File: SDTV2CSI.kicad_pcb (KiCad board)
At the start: 4 copper layers, 65 x 21 mm, 43 parts, among them J1 Conn_Coaxial, J2 Conn_Coaxial, J3 SFW15R-1STE1LF, U1 ADV7280AWBCPZ-M, U2 TLV75718PDBV, Y1 28.63636MHz

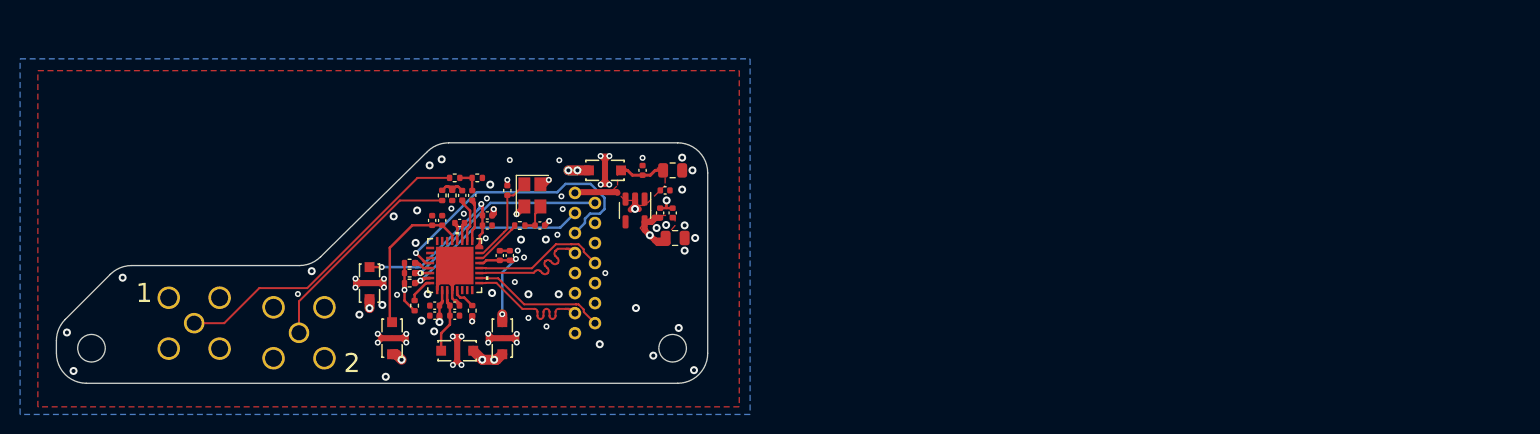
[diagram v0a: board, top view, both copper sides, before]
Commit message: update and considering losing poe for waveshare OTS
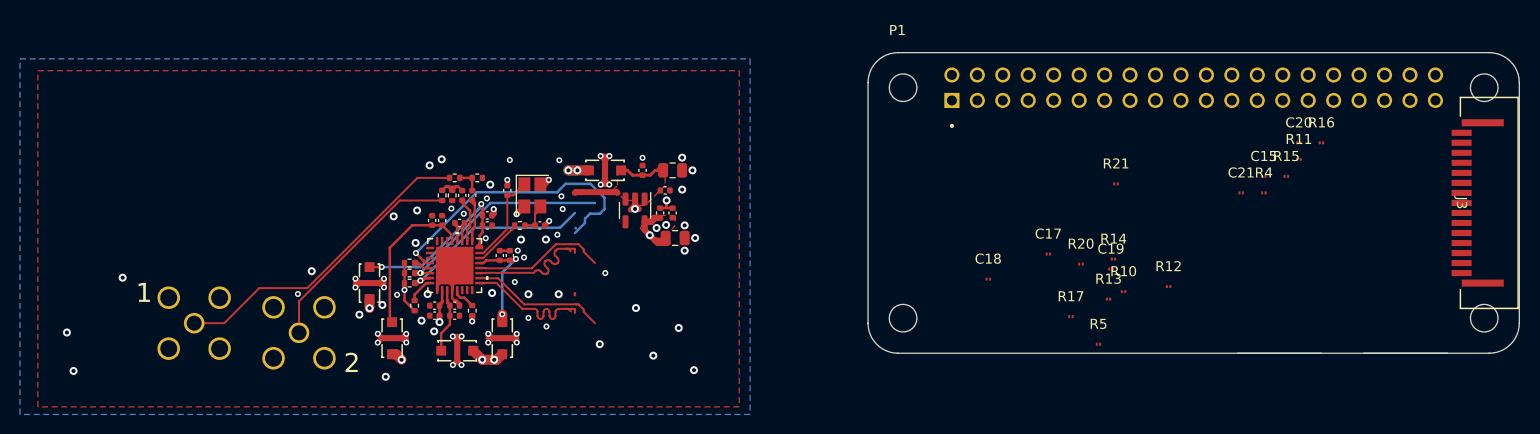
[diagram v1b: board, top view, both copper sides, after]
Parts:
- removed REF**: MODULE_ADA3708, AU:PIZERO_OUTLINE
- added C15: 0.1μF, AU:R_0201_0603Metric, F.Cu at (219.2, 52.4)
- added C17: 0.1μF, AU:R_0201_0603Metric, F.Cu at (197.8, 60.1)
- added C18: 0.1μF, AU:R_0201_0603Metric, F.Cu at (191.8, 62.6)
- added C19: 0.1μF, AU:R_0201_0603Metric, F.Cu at (204.0, 61.6)
- added C20: 0.1μF, AU:R_0201_0603Metric, F.Cu at (222.8, 49.0)
- added C21: 0.1μF, AU:R_0201_0603Metric, F.Cu at (217.0, 54.0)
- added P1: Pi Zero, AU:PIZERO, F.Cu at (212.2, 55.0)
- added R10: 24, Resistor_SMD:R_0201_0603Metric, F.Cu at (205.2, 63.9)
- added R11: 51, Resistor_SMD:R_0201_0603Metric, F.Cu at (222.8, 50.6)
- added R12: 24, Resistor_SMD:R_0201_0603Metric, F.Cu at (209.8, 63.4)
- added R13: 51, Resistor_SMD:R_0201_0603Metric, F.Cu at (203.8, 64.6)
- added R14: 24, Resistor_SMD:R_0201_0603Metric, F.Cu at (204.2, 60.6)
- added R15: 51, Resistor_SMD:R_0201_0603Metric, F.Cu at (221.5, 52.4)
- added R16: 24, Resistor_SMD:R_0201_0603Metric, F.Cu at (225.0, 49.0)
- added R17: 51, Resistor_SMD:R_0201_0603Metric, F.Cu at (200.0, 66.3)
- added R20: 24, Resistor_SMD:R_0201_0603Metric, F.Cu at (201.0, 61.1)
- added R21: 51, Resistor_SMD:R_0201_0603Metric, F.Cu at (204.5, 53.1)
- added R4: 24, Resistor_SMD:R_0201_0603Metric, F.Cu at (219.2, 54.0)
- added R5: 51, Resistor_SMD:R_0201_0603Metric, F.Cu at (202.8, 69.1)
- J3: footprint AU:528061510 -> AU:CON15_1X15_DRB_SFW_GLE; moved to F.Cu
- moved J3 90.4 mm to (241.8, 55.0), turned to -90 degrees
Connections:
- net SCL renamed CSCL
- net SDA renamed CSDA
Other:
- board size 65 x 21 mm -> 65 x 30 mm

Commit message: working on converting back to 0201
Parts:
- added J4: Conn_Coaxial, Connector_Coaxial:SMA_Amphenol_901-144_Vertical, F.Cu at (207.2, 97.8)
- added J5: Conn_Coaxial, Connector_Coaxial:SMA_Amphenol_901-144_Vertical, F.Cu at (178.8, 123.5)
- added J6: Conn_Coaxial, Connector_Coaxial:SMA_Amphenol_901-144_Vertical, F.Cu at (207.2, 107.2)
- added J7: Conn_Coaxial, Connector_Coaxial:SMA_Amphenol_901-144_Vertical, F.Cu at (196.2, 113.0)
- added J8: Conn_Coaxial, Connector_Coaxial:SMA_Amphenol_901-144_Vertical, F.Cu at (188.1, 122.4)
- added J9: Conn_Coaxial, Connector_Coaxial:SMA_Amphenol_901-144_Vertical, F.Cu at (186.9, 113.0)
- added R27: 4.7k, Resistor_SMD:R_0402_1005Metric, F.Cu at (162.5, 85.5)
- added R28: 4.7k, Resistor_SMD:R_0402_1005Metric, F.Cu at (144.1, 94.5)
- added R29: 4.7k, Resistor_SMD:R_0402_1005Metric, F.Cu at (138.2, 94.5)
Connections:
- U1 pad 6: unconnected-(U1-Pad6) -> Net-(U1-Pad6)
- U1 pad 7: unconnected-(U1-Pad7) -> Net-(U1-Pad7)
- U1 pad 8: unconnected-(U1-Pad8) -> Net-(U1-Pad8)

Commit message: will remove PoE components commit for posterity
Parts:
- C1, C10, C11, C12, C13, C14, C16, C2, C3, C4, C5, C6, C7, C8, C9: footprint Capacitor_SMD:C_0402_1005Metric -> AU:R_0201_0603Metric
- J3: moved to B.Cu
- R1, R2, R24, R25, R26, R27, R28, R29, R3, R6, R7, R9: footprint Resistor_SMD:R_0402_1005Metric -> Resistor_SMD:R_0201_0603Metric
- R23: footprint Resistor_SMD:R_0402_1005Metric -> AU:R_0201_0603Metric
- U2: value TLV75718PDBV -> TLV75718
- turned J3 to 90 degrees
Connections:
- C10 pad 1: GND -> PVDD
- C10 pad 2: PVDD -> GND
- C12 pad 1: GND -> AVDD
- C12 pad 2: AVDD -> GND
- C13 pad 1: Net-(C13-Pad1) -> Net-(U1-Pad20)
- C13 pad 2: Net-(C13-Pad2) -> Net-(U1-Pad19)
- C14 pad 2: Net-(C14-Pad2) -> Net-(R2-Pad2)
- C15 pad 2: Net-(C15-Pad2) -> Net-(R5-Pad2)
- C16 pad 2: Net-(C16-Pad2) -> Net-(R9-Pad2)
- C2 pad 1: GND -> DVDDIO
- C2 pad 2: DVDDIO -> GND
- C5 pad 1: GND -> MVDD
- C5 pad 2: MVDD -> GND
- C8 pad 1: GND -> DVDD
- C8 pad 2: DVDD -> GND
- J3 pad 1: GND -> +3V3
- J3 pad 10: GND -> CD1+
- J3 pad 11: PWR_EN -> CD1-
- J3 pad 12: LED_EN -> GND
- J3 pad 13: CSCL -> CD0+
- J3 pad 14: CSDA -> CD0-
- J3 pad 15: +3V3 -> GND
- J3 pad 2: CD0- -> CSDA
- J3 pad 3: CD0+ -> CSCL
- J3 pad 4: GND -> LED_EN
- J3 pad 5: CD1- -> PWR_EN
- J3 pad 6: CD1+ -> GND
- J3 pad 7: GND -> CLK+
- J3 pad 9: CLK+ -> GND
- R1 pad 1: Net-(R1-Pad1) -> DVDDIO
- R1 pad 2: DVDDIO -> Net-(U1-Pad29)
- R11 pad 1: Net-(C17-Pad2) -> GND
- R11 pad 2: GND -> Net-(C17-Pad2)
- R13 pad 1: Net-(C18-Pad2) -> GND
- R13 pad 2: GND -> Net-(C18-Pad2)
- R15 pad 1: Net-(C19-Pad2) -> GND
- R15 pad 2: GND -> Net-(C19-Pad2)
- R17 pad 1: Net-(C20-Pad2) -> GND
- R17 pad 2: GND -> Net-(C20-Pad2)
- R2 pad 2: Net-(C14-Pad2) -> Net-(R2-Pad2)
- R21 pad 1: Net-(C21-Pad2) -> GND
- R21 pad 2: GND -> Net-(C21-Pad2)
- R25 pad 1: CSDA -> DVDDIO
- R25 pad 2: DVDDIO -> CSDA
- R26 pad 1: INTRQ -> DVDDIO
- R26 pad 2: DVDDIO -> INTRQ
- R27 pad 1: Net-(U1-Pad7) -> Net-(R27-Pad1)
- R28 pad 1: Net-(U1-Pad6) -> Net-(R28-Pad1)
- R29 pad 1: Net-(U1-Pad8) -> GND
- R29 pad 2: GND -> Net-(U1-Pad8)
- R3 pad 1: Net-(C14-Pad2) -> GND
- R3 pad 2: GND -> Net-(R2-Pad2)
- R4 pad 2: Net-(C15-Pad2) -> Net-(R5-Pad2)
- R5 pad 1: Net-(C15-Pad2) -> GND
- R5 pad 2: GND -> Net-(R5-Pad2)
- R7 pad 2: Net-(C16-Pad2) -> Net-(R9-Pad2)
- R9 pad 1: Net-(C16-Pad2) -> GND
- R9 pad 2: GND -> Net-(R9-Pad2)
- U1 pad 19: Net-(C13-Pad1) -> Net-(U1-Pad19)
- U1 pad 20: Net-(C13-Pad2) -> Net-(U1-Pad20)
- U1 pad 29: Net-(R1-Pad1) -> Net-(U1-Pad29)
- U1 pad 6: Net-(U1-Pad6) -> Net-(R27-Pad1)
- U1 pad 7: Net-(U1-Pad7) -> Net-(R28-Pad1)
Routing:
- net DVDDIO: track 50.4 -> 72.8 mm, vias 5 -> 6
- net CSDA: track 22.4 -> 0.00 mm, vias 1 -> 0
- net Net-(U1-Pad29): track 0.00 -> 2.54 mm
- net Net-(R1-Pad1): track 2.54 -> 0.00 mm
- net Net-(U1-Pad20): track 0.00 -> 2.46 mm
- net Net-(C13-Pad2): track 2.46 -> 0.00 mm
- net Net-(U1-Pad19): track 0.00 -> 2.31 mm
- net Net-(C13-Pad1): track 2.31 -> 0.00 mm
- net PVDD: track 21.0 -> 21.8 mm
- net GND: track 52.0 -> 51.2 mm

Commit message: updating for GitHub
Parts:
- removed J3: SFW15R-1STE1LF, AU:CON15_1X15_DRB_SFW_GLE
- removed J4, J5, J6, J7, J8: Conn_Coaxial, Connector_Coaxial:SMA_Amphenol_901-144_Vertical
- added D1: TVS, AU:R_0201_0603Metric, F.Cu at (103.8, 96.2)
- added D10: TVS, AU:R_0201_0603Metric, F.Cu at (103.8, 97.9)
- added D11: TVS, AU:R_0201_0603Metric, F.Cu at (106.0, 97.9)
- added D12: TVS, AU:R_0201_0603Metric, F.Cu at (108.2, 99.5)
- added D13: TVS, AU:R_0201_0603Metric, F.Cu at (103.4, 102.8)
- added D14: TVS, AU:R_0201_0603Metric, F.Cu at (108.2, 97.9)
- added D15: TVS, AU:R_0201_0603Metric, F.Cu at (108.2, 96.2)
- added D16: TVS, AU:R_0201_0603Metric, F.Cu at (103.4, 101.2)
- added D17: TVS, AU:R_0201_0603Metric, F.Cu at (105.6, 101.2)
- added D18: LED_Dual_AAK, Package_TO_SOT_SMD:SOT-23, F.Cu at (98.0, 96.5)
- added D2: TVS, AU:R_0201_0603Metric, F.Cu at (106.0, 96.2)
- added D3: TVS, AU:R_0201_0603Metric, F.Cu at (106.0, 99.5)
- added D4: TVS, AU:R_0201_0603Metric, F.Cu at (98.9, 102.3)
- added D5: 3VWM, AU:R_0201_0603Metric, F.Cu at (101.1, 102.3)
- added D6: 3VWM, AU:R_0201_0603Metric, F.Cu at (98.9, 100.7)
- added D7: 3VWM, AU:R_0201_0603Metric, F.Cu at (103.8, 99.5)
- added D8: 3VWM, AU:R_0201_0603Metric, F.Cu at (101.1, 100.7)
- added D9: 3VWM, AU:R_0201_0603Metric, F.Cu at (110.5, 96.2)
- added R18: 560, AU:R_0201_0603Metric, F.Cu at (95.2, 96.5)
- added R19: 220, AU:R_0201_0603Metric, F.Cu at (95.2, 97.2)
- added R8: 560, AU:R_0201_0603Metric, F.Cu at (95.2, 95.8)
- added U3: TCA9555RGER, Package_DFN_QFN:VQFN-24-1EP_4x4mm_P0.5mm_EP2.45x2.45mm, F.Cu at (193.7, 27.8)
- added U4: TS3DS10224RUK, Package_DFN_QFN:WQFN-20-1EP_3x3mm_P0.4mm_EP1.7x1.7mm_ThermalVias, F.Cu at (206.0, 31.0)
- added U5: TS3DS10224RUK, Package_DFN_QFN:WQFN-20-1EP_3x3mm_P0.4mm_EP1.7x1.7mm_ThermalVias, F.Cu at (200.7, 25.7)
- added U6: TS3DS10224RUK, Package_DFN_QFN:WQFN-20-1EP_3x3mm_P0.4mm_EP1.7x1.7mm_ThermalVias, F.Cu at (200.7, 31.0)
- added U7: TS3DS10224RUK, Package_DFN_QFN:WQFN-20-1EP_3x3mm_P0.4mm_EP1.7x1.7mm_ThermalVias, F.Cu at (206.0, 25.7)
- F1, F2, F3, F4, F5: value LC(PI) -> LC(Pi); footprint AU:NFE31PT101C1E9L_MUR -> AU:MEM1608P25R0T001
- J1, J2: value Conn_Coaxial -> SMA
- J9: value Conn_Coaxial -> SFW15R-1STE1LF; footprint Connector_Coaxial:SMA_Amphenol_901-144_Vertical -> AU:CON15_1X15_DRB_SFW_GLE
- P1: moved to B.Cu
- moved J9 75.8 mm to (235.8, 55.0), turned to -90 degrees
- moved C12 49.4 mm to (185.0, 48.8), turned to 0 degrees
- moved C11 47.4 mm to (184.0, 49.0)
- moved C2 46.9 mm to (182.8, 58.2), turned to 180 degrees
- moved C1 46.9 mm to (182.8, 57.5)
- moved U1 46.6 mm to (184.5, 53.5)
- moved C13 46.6 mm to (185.0, 49.5), turned to 0 degrees
- moved C8 46.4 mm to (184.2, 58.2), turned to 0 degrees
- moved C6 46.4 mm to (184.2, 57.5)
- moved C9 46.2 mm to (187.2, 49.5)
- moved C10 46.1 mm to (187.2, 48.8)
- moved C3 45.9 mm to (188.2, 52.8)
- moved C5 45.6 mm to (189.0, 52.8)
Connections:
- F1 pad 1: DVDDIO -> +3V3
- F1 pad 3: +3V3 -> DVDDIO
- F2 pad 1: MVDD -> +1V8
- F2 pad 3: +1V8 -> MVDD
- F3 pad 1: DVDD -> +1V8
- F3 pad 3: +1V8 -> DVDD
- F4 pad 1: PVDD -> +1V8
- F4 pad 3: +1V8 -> PVDD
- F5 pad 1: AVDD -> +1V8
- F5 pad 3: +1V8 -> AVDD
- J9 pad 1: video_in4 -> +3V3
- J9 pad 2: GND -> CSDA
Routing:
- net AVDD: track 15.7 -> 11.3 mm
- net video2: track 4.95 -> 1.17 mm
- net video1: track 4.79 -> 1.05 mm
- net Net-(C16-Pad2) (its old number): track 3.55 -> 0.00 mm
- net video_in1: track 31.5 -> 28.3 mm
- net Net-(C14-Pad2) (its old number): track 2.50 -> 0.00 mm
- net Net-(C13-Pad1): track 2.46 -> 1.18 mm
- net Net-(C13-Pad2): track 2.31 -> 1.38 mm
- net PVDD: track 21.8 -> 21.0 mm
- net GND: track 51.2 -> 52.0 mm, vias 77 -> 76

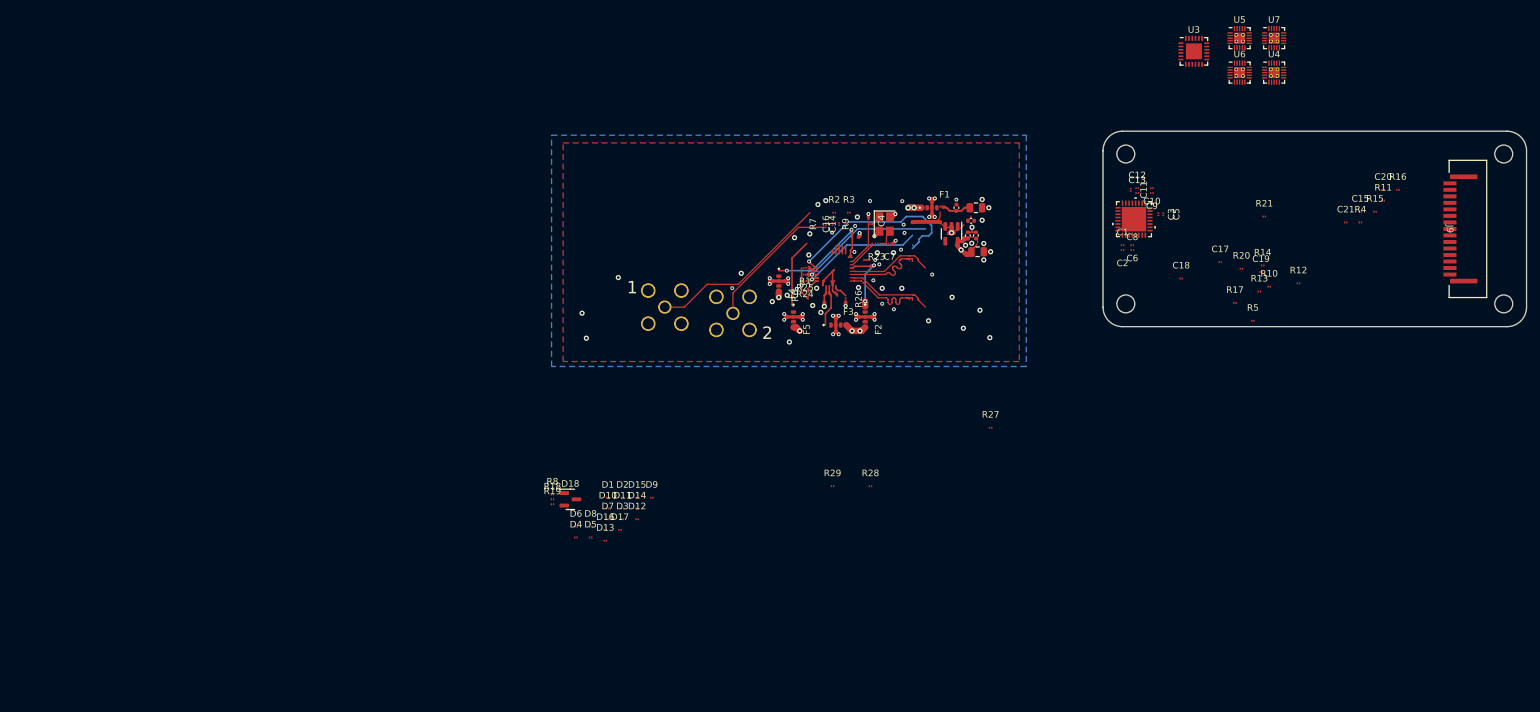
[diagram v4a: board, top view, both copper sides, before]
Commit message: latest iteration with smaller filters and bigger more secure footprint
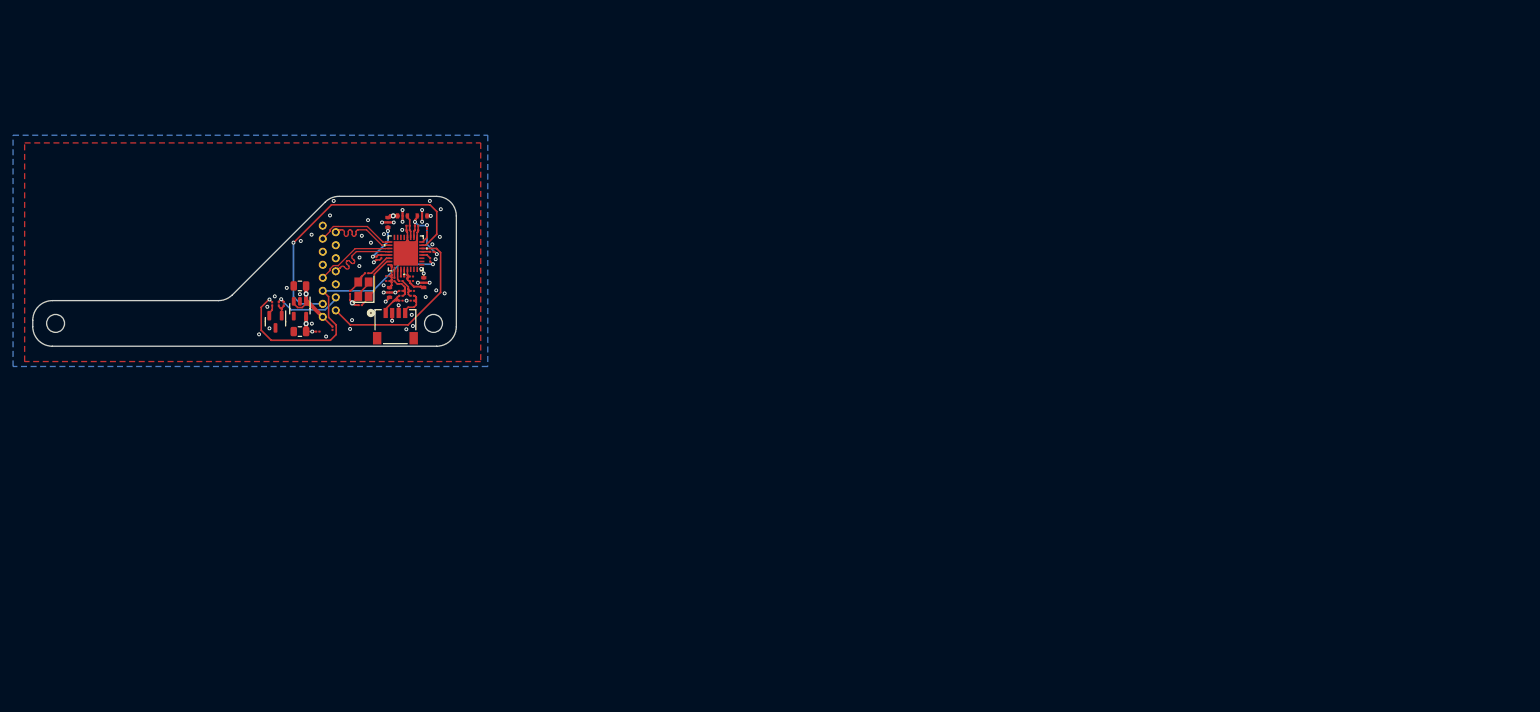
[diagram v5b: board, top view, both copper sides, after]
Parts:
- removed C18, C19, C20, C21: 0.1μF, AU:R_0201_0603Metric
- removed C22, C23: 100μF, Capacitor_SMD:C_0805_2012Metric
- removed C24, C27: 0.01μF, Capacitor_SMD:C_0402_1005Metric
- removed C25, C26: 0.1μF, Capacitor_SMD:C_0402_1005Metric
- removed D10, D11, D12, D13, D14, D15, D16, D17: TVS, AU:R_0201_0603Metric
- removed D18: LED_Dual_AAK, Package_TO_SOT_SMD:SOT-23
- removed D6, D7, D8, D9: 3VWM, AU:R_0201_0603Metric
- removed the J2 at (123.0, 68.0)
- removed R12, R14, R16, R20: 24, Resistor_SMD:R_0201_0603Metric
- removed R13, R15, R17, R21: 51, Resistor_SMD:R_0201_0603Metric
- removed R18, R23: 560, AU:R_0201_0603Metric
- removed R19: 220, AU:R_0201_0603Metric
- removed R24, R25, R26, R27, R28, R29: 4.7k, Resistor_SMD:R_0201_0603Metric
- removed U3: TCA9555RGER, Package_DFN_QFN:VQFN-24-1EP_4x4mm_P0.5mm_EP2.45x2.45mm
- removed U4, U5, U6, U7: TS3DS10224RUK, Package_DFN_QFN:WQFN-20-1EP_3x3mm_P0.4mm_EP1.7x1.7mm_ThermalVias
- C11, C6: value 0.01μF -> 0.1μF
- C14, C15: value 0.1μF -> 100μF; footprint AU:R_0201_0603Metric -> Capacitor_SMD:C_0805_2012Metric
- C16, C17: value 0.1μF -> 20pF
- C4: value 20pF -> 0.1μF
- C5: value 0.1μF -> 0.01μF
- C7: value 20pF -> 0.01μF
- D1: value TVS -> 3VWM
- D2: value TVS -> 2VWM
- D5: value 3VWM -> LED_Dual_AAK; footprint AU:R_0201_0603Metric -> Package_TO_SOT_SMD:SOT-23
- J1: renamed from J9; footprint AU:CON15_1X15_DRB_SFW_GLE -> AU:528061510; moved to B.Cu
- J2: renamed from J1; value SMA -> SM04B-SRSS-TB; footprint Connector_Coaxial:SMA_Amphenol_901-144_Vertical -> AU:SM04B-SRSS-TB_JST; moved to F.Cu
- R1: value 4.7k -> 24; footprint Resistor_SMD:R_0201_0603Metric -> AU:R_0201_0603Metric
- R10: value 24 -> 560; footprint Resistor_SMD:R_0201_0603Metric -> AU:R_0201_0603Metric
- R11: value 51 -> 220; footprint Resistor_SMD:R_0201_0603Metric -> AU:R_0201_0603Metric
- R2, R4: value 24 -> 51; footprint Resistor_SMD:R_0201_0603Metric -> AU:R_0201_0603Metric
- R3: value 51 -> 24; footprint Resistor_SMD:R_0201_0603Metric -> AU:R_0201_0603Metric
- R5: value 51 -> 4.7k; footprint Resistor_SMD:R_0201_0603Metric -> AU:R_0201_0603Metric
- R6: footprint Resistor_SMD:R_0201_0603Metric -> AU:R_0201_0603Metric
- R7: value 24 -> 4.7k; footprint Resistor_SMD:R_0201_0603Metric -> AU:R_0201_0603Metric
- R9: value 51 -> 560; footprint Resistor_SMD:R_0201_0603Metric -> AU:R_0201_0603Metric
- moved J1 174.9 mm to (61.0, 61.5), turned to 90 degrees
- moved R11 171.2 mm to (52.2, 66.5), turned to 90 degrees
- moved P1 164.3 mm to (48.0, 58.0), turned to 180 degrees
- moved C15 163.8 mm to (56.5, 70.8)
- moved R10 151.3 mm to (54.0, 66.5), turned to 90 degrees
- moved R4 145.9 mm to (73.8, 64.5), turned to 180 degrees
- moved C17 133.6 mm to (64.2, 64.8), turned to 90 degrees
- moved R5 126.6 mm to (76.5, 59.8), turned to -90 degrees
- moved C3 119.4 mm to (69.0, 59.2), turned to 90 degrees
- moved C5 115.9 mm to (73.1, 55.2), turned to 0 degrees
- moved C10 114.5 mm to (73.6, 63.0), turned to 0 degrees
- moved C9 114.4 mm to (73.6, 62.3)
- moved C8 114.3 mm to (70.0, 63.0), turned to 180 degrees
- moved C12 113.9 mm to (72.0, 63.0)
- moved C11 113.8 mm to (71.0, 62.8)
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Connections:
- C10 pad 1: PVDD -> AVDD
- C11 pad 1: GND -> video1
- C11 pad 2: AVDD -> Net-(C11-Pad2)
- C12 pad 1: AVDD -> video2
- C12 pad 2: GND -> Net-(C12-Pad2)
- C14 pad 1: video1 -> GND
- C14 pad 2: Net-(C14-Pad2) -> +3V3
- C15 pad 1: video5 -> GND
- C15 pad 2: Net-(C15-Pad2) -> +1V8
- C16 pad 1: video2 -> GND
- C16 pad 2: Net-(C16-Pad2) -> XN
- C17 pad 1: video6 -> GND
- C4 pad 1: GND -> MVDD
- C4 pad 2: XN -> GND
- C5 pad 1: MVDD -> GND
- C5 pad 2: GND -> DVDD
- C6 pad 1: GND -> DVDD
- C6 pad 2: DVDD -> GND
- C7 pad 2: Net-(C7-Pad2) -> PVDD
- C8 pad 1: DVDD -> PVDD
- C9 pad 2: PVDD -> AVDD
- D1 pad 1: CLK+ -> +3V3
- D2 pad 1: CLK- -> +1V8
- D3 pad 1: CD0+ -> video_in1
- D4 pad 1: CD0- -> video_in2
- D5 pad 1: +3V3 -> Net-(D5-Pad1)
- D5 pad 2: GND -> Net-(D5-Pad2)
- J1 pad 4: RESET -> LED_EN
- R1 pad 1: DVDDIO -> video_in1
- R1 pad 2: Net-(R1-Pad2) -> Net-(C11-Pad2)
- R10 pad 1: video_in6 -> Net-(D5-Pad1)
- R10 pad 2: Net-(C17-Pad2) -> LED_EN
- R11 pad 1: GND -> Net-(D5-Pad2)
- R11 pad 2: Net-(C17-Pad2) -> PWR_EN
- R2 pad 1: video_in1 -> GND
- R2 pad 2: Net-(C14-Pad2) -> Net-(C11-Pad2)
- R3 pad 1: GND -> video_in2
- R3 pad 2: Net-(C14-Pad2) -> Net-(C12-Pad2)
- R4 pad 1: video_in5 -> GND
- R4 pad 2: Net-(C15-Pad2) -> Net-(C12-Pad2)
- R5 pad 1: GND -> Net-(R5-Pad1)
- R5 pad 2: Net-(C15-Pad2) -> PWR_EN
- R7 pad 1: video_in2 -> DVDDIO
- R7 pad 2: Net-(C16-Pad2) -> Net-(R7-Pad2)
- R8 pad 1: Net-(D18-Pad1) -> Net-(C17-Pad2)
- R8 pad 2: LED_EN -> XP
- R9 pad 1: GND -> Net-(D5-Pad1)
- R9 pad 2: Net-(C16-Pad2) -> LED_EN
- U1 pad 22: video3 -> unconnected-(U1-Pad22)
- U1 pad 23: video4 -> unconnected-(U1-Pad23)
- U1 pad 24: video5 -> unconnected-(U1-Pad24)
- U1 pad 25: video6 -> unconnected-(U1-Pad25)
- U1 pad 26: video7 -> unconnected-(U1-Pad26)
- U1 pad 27: video8 -> unconnected-(U1-Pad27)
- U1 pad 28: PWR_EN -> Net-(R5-Pad1)
- U1 pad 29: Net-(R1-Pad2) -> Net-(R7-Pad2)
- U1 pad 5: INTRQ -> unconnected-(U1-Pad5)
- U1 pad 6: Net-(R27-Pad1) -> unconnected-(U1-Pad6)
- U1 pad 7: Net-(R28-Pad1) -> unconnected-(U1-Pad7)
- U1 pad 8: Net-(R29-Pad2) -> unconnected-(U1-Pad8)
- Y1 pad 3: Net-(C7-Pad2) -> Net-(C17-Pad2)
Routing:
- net DVDDIO: track 72.8 -> 12.0 mm, vias 6 -> 3
- net +3V3: track 8.95 -> 42.7 mm, vias 0 -> 2
- net CSDA: track 0.00 -> 28.3 mm
- net video_in1: track 28.3 -> 5.31 mm
- net CSCL: track 22.0 -> 44.6 mm
- net GND: track 52.0 -> 30.3 mm, vias 76 -> 49
- net video_in2: track 21.6 -> 4.26 mm
- net PVDD: track 21.0 -> 5.09 mm, vias 2 -> 0
- net PWR_EN: track 29.5 -> 45.2 mm, vias 1 -> 2
- net LED_EN: track 0.00 -> 11.3 mm, vias 0 -> 1
- net AVDD: track 11.3 -> 5.44 mm
- net +1V8: track 12.3 -> 6.87 mm, vias 7 -> 5
- net Net-(C11-Pad2): track 0.00 -> 4.18 mm
- net DVDD: track 7.05 -> 3.26 mm
- net Net-(C12-Pad2): track 0.00 -> 3.63 mm
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- removed copper zone on F.Cu, net +1V8
- removed copper zone on F.Cu, net +3V3
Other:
- board size 65 x 30 mm -> 65 x 20 mm
- board text removed: "1"
- board text removed: "2"
